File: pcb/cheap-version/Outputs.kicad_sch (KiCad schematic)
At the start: 21 parts, among them J501 FAN1 / 3.5 mm, J511 FAN2 / 3.5 mm, J521 PUMP 24V / 6W, Q501 AO3400A, Q511 AO3400A, Q521 AO3422

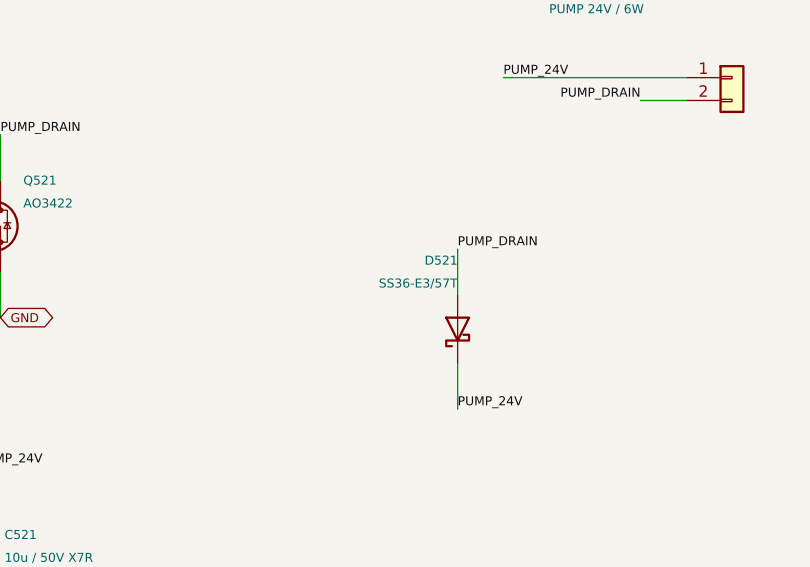
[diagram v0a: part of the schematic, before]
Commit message: cheap-version: schematic substitutions from stock parts
tools/make_cheap1.py generates the cheap-1 sheets from the PCB_V1 0.22 baseline:
ST1S14 for LMR16020 (RT resistor removed, EN/FB divider recalculated), IRS4427S and
IRL2505 for the heater, BSC146N10LS5 for the LED boost switches, SS56 diodes,
KF301/FS1.5/KF2510/XH connectors, stock resistors and capacitors (Source field =
stock:<id>). J901 XT60 is replaced by a screw terminal as decided. U101 TPS54202 and
D711/D721 SS5P10 are kept because datasheets for ST1S10 and SBRT15U100SP5 were not
available. ERC: 0 errors (one warning: footprint for the DTMSS-27 inductor pending);
netdiff against PCB_V1: no connectivity differences among untouched pins.

Co-Authored-By: Claude Sonnet 5.5 <noreply@anthropic.com>
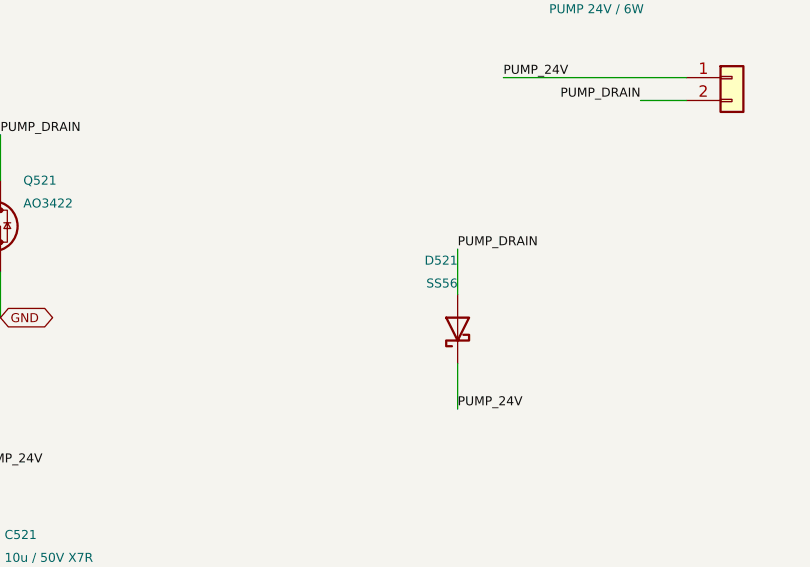
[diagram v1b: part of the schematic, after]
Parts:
- C521: LCSC C386166 -> C92388; MPN UMK325AB7106KMHP -> CL32B106KBJNNNE; Manufacturer Taiyo Yuden -> Samsung Electro-Mechanics; Source (none) -> stock:47
- D521: value SS36-E3/57T -> SS56; LCSC C35722 -> (none); MPN SS36-E3/57T -> SS56; Manufacturer Vishay -> (none); Source (none) -> stock:20
- J501, J511: footprint GrowBox:TerminalBlock_DORABO_DB125-3.5_1x04_P3.50mm_Horizontal -> Connector_Molex:Molex_KK-254_AE-6410-04A_1x04_P2.54mm_Vertical; LCSC C2757925 -> (none); MPN DB125-3.5-4P-GN-S -> KF2510-4P; Manufacturer DORABO -> (none); Source (none) -> stock:87
- J521: footprint GrowBox:TerminalBlock_DORABO_DB125-3.5_1x02_P3.50mm_Horizontal -> TerminalBlock_Phoenix:TerminalBlock_Phoenix_PT-1,5-2-3.5-H_1x02_P3.50mm_Horizontal; LCSC C466970 -> (none); MPN DB125-3.5-2P-GN-S -> FS1.5-02-350-2601R; Manufacturer DORABO -> (none); Source (none) -> stock:86
- R502, R512, R522: LCSC C25803 -> C14675; MPN 0603WAF1003T5E -> RC0603FR-07100KL; Manufacturer UNI-ROYAL -> Yageo; Source (none) -> stock:55
- R503, R513: MPN 0603WAF1001T5E -> RC0603FR-071KL; Manufacturer UNI-ROYAL -> Yageo; Source (none) -> stock:62
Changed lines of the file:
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@@
 	(title_block
 		(title "04 - Fans (12 V aux) and pump (24 V)")
-		(date "2026-09-30")
-		(rev "0.22-DRAFT")
+		(date "2026-10-03")
+		(rev "cheap-1-DRAFT")
 		(company "GrowBox controller")
-		(comment 1 "Simplified prototype; unrouted; hardware qualification pending")
+		(comment 1 "cheap-1: one-off board from stock parts, schematic derived from PCB_V1 0.22; unrouted")
 	)
 	(text "04  PTC 100 W — отдельный лист Heater"
@@
 			)
 		)
-		(property "Manufacturer" "UNI-ROYAL"
+		(property "Manufacturer" "Yageo"
 			(at 50.8 231.14 0)
 			(hide yes)
@@
 			)
 		)
-		(property "MPN" "0603WAF1003T5E"
+		(property "MPN" "RC0603FR-07100KL"
 			(at 50.8 231.14 0)
 			(hide yes)
@@
 			)
 		)
-		(property "LCSC" "C25803"
+		(property "LCSC" "C14675"
 			(at 50.8 231.14 0)
 			(hide yes)
@@
 					(size 1 1)
 				)
+				(justify left)
+			)
+		)
+		(property "Source" "stock:55"
+			(at 50.8 231.14 0)
+			(effects
+				(font
+					(size 1 1)
+				)
+				(hide yes)
 				(justify left)
 			)
@@
 			)
 		)
-		(property "Value" "SS36-E3/57T"
+		(property "Value" "SS56"
 			(at 154.94 214.63 90)
 			(show_name no)
@@
 			)
 		)
-		(property "LCSC" "C35722"
+		(property "LCSC" ""
 			(at 154.94 219.71 0)
 			(effects
@@
 			)
 		)
-		(property "MPN" "SS36-E3/57T"
+		(property "Source" "stock:20"
+			(at 154.94 219.71 90)
+			(effects
+				(font
+					(size 1 1)
+				)
+				(hide yes)
+				(justify left)
+			)
+		)
+		(property "MPN" "SS56"
 			(at 154.94 219.71 0)
 			(effects
@@
 			)
 		)
-		(property "Manufacturer" "Vishay"
+		(property "Manufacturer" ""
 			(at 154.94 219.71 0)
 			(effects
@@
 			)
 		)
-		(property "Footprint" "GrowBox:TerminalBlock_DORABO_DB125-3.5_1x04_P3.50mm_Horizontal"
+		(property "Footprint" "Connector_Molex:Molex_KK-254_AE-6410-04A_1x04_P2.54mm_Vertical"
 			(at 182.88 60.96 0)
 			(hide yes)
@@
 			)
 		)
-		(property "LCSC" "C2757925"
+		(property "LCSC" ""
 			(at 182.88 60.96 0)
 			(effects
@@
 			)
 		)
-		(property "MPN" "DB125-3.5-4P-GN-S"
+		(property "Source" "stock:87"
 			(at 182.88 60.96 0)
 			(effects
@@
 			)
 		)
-		(property "Manufacturer" "DORABO"
+		(property "MPN" "KF2510-4P"
+			(at 182.88 60.96 0)
+			(effects
+				(font
+					(size 1 1)
+				)
+				(hide yes)
+				(justify left)
+			)
+		)
+		(property "Manufacturer" ""
 			(at 182.88 60.96 0)
 			(effects
@@
 			)
 		)
-		(property "Manufacturer" "UNI-ROYAL"
+		(property "Manufacturer" "Yageo"
 			(at 50.8 93.98 0)
 			(hide yes)
@@
 			)
 		)
-		(property "MPN" "0603WAF1003T5E"
+		(property "MPN" "RC0603FR-07100KL"
 			(at 50.8 93.98 0)
 			(hide yes)
@@
 			)
 		)
-		(property "LCSC" "C25803"
+		(property "LCSC" "C14675"
 			(at 50.8 93.98 0)
 			(hide yes)
@@
 					(size 1 1)
 				)
+				(justify left)
+			)
+		)
+		(property "Source" "stock:55"
+			(at 50.8 93.98 0)
+			(effects
+				(font
+					(size 1 1)
+				)
+				(hide yes)
 				(justify left)
 			)
@@
 			)
 		)
-		(property "Footprint" "GrowBox:TerminalBlock_DORABO_DB125-3.5_1x02_P3.50mm_Horizontal"
+		(property "Footprint" "TerminalBlock_Phoenix:TerminalBlock_Phoenix_PT-1,5-2-3.5-H_1x02_P3.50mm_Horizontal"
 			(at 185.42 191.77 0)
 			(hide yes)
@@
 			)
 		)
-		(property "LCSC" "C466970"
+		(property "LCSC" ""
 			(at 185.42 191.77 0)
 			(effects
@@
 			)
 		)
-		(property "MPN" "DB125-3.5-2P-GN-S"
+		(property "Source" "stock:86"
 			(at 185.42 191.77 0)
 			(effects
@@
 			)
 		)
-		(property "Manufacturer" "DORABO"
+		(property "MPN" "FS1.5-02-350-2601R"
+			(at 185.42 191.77 0)
+			(effects
+				(font
+					(size 1 1)
+				)
+				(hide yes)
+				(justify left)
+			)
+		)
+		(property "Manufacturer" ""
 			(at 185.42 191.77 0)
 			(effects
@@
 			)
 		)
-		(property "Footprint" "GrowBox:TerminalBlock_DORABO_DB125-3.5_1x04_P3.50mm_Horizontal"
+		(property "Footprint" "Connector_Molex:Molex_KK-254_AE-6410-04A_1x04_P2.54mm_Vertical"
 			(at 381 60.96 0)
 			(hide yes)
@@
 			)
 		)
-		(property "LCSC" "C2757925"
+		(property "LCSC" ""
 			(at 381 60.96 0)
 			(effects
@@
 			)
 		)
-		(property "MPN" "DB125-3.5-4P-GN-S"
+		(property "Source" "stock:87"
 			(at 381 60.96 0)
 			(effects
@@
 			)
 		)
-		(property "Manufacturer" "DORABO"
+		(property "MPN" "KF2510-4P"
+			(at 381 60.96 0)
+			(effects
+				(font
+					(size 1 1)
+				)
+				(hide yes)
+				(justify left)
+			)
+		)
+		(property "Manufacturer" ""
 			(at 381 60.96 0)
 			(effects
@@
 			)
 		)
-		(property "Manufacturer" "UNI-ROYAL"
+		(property "Manufacturer" "Yageo"
 			(at 302.26 109.22 90)
 			(hide yes)
@@
 			)
 		)
-		(property "MPN" "0603WAF1001T5E"
+		(property "MPN" "RC0603FR-071KL"
 			(at 302.26 109.22 90)
 			(hide yes)
@@
 					(size 1 1)
 				)
+				(justify left)
+			)
+		)
+		(property "Source" "stock:62"
+			(at 302.26 109.22 90)
+			(effects
+				(font
+					(size 1 1)
+				)
+				(hide yes)
 				(justify left)
 			)
@@
 			)
 		)
-		(property "Manufacturer" "UNI-ROYAL"
+		(property "Manufacturer" "Yageo"
 			(at 248.92 93.98 0)
 			(hide yes)
@@
 			)
 		)
-		(property "MPN" "0603WAF1003T5E"
+		(property "MPN" "RC0603FR-07100KL"
 			(at 248.92 93.98 0)
 			(hide yes)
@@
 			)
 		)
-		(property "LCSC" "C25803"
+		(property "LCSC" "C14675"
 			(at 248.92 93.98 0)
 			(hide yes)
@@
 					(size 1 1)
 				)
+				(justify left)
+			)
+		)
+		(property "Source" "stock:55"
+			(at 248.92 93.98 0)
+			(effects
+				(font
+					(size 1 1)
+				)
+				(hide yes)
 				(justify left)
 			)
@@
 			)
 		)
-		(property "Manufacturer" "UNI-ROYAL"
+		(property "Manufacturer" "Yageo"
 			(at 104.14 109.22 90)
 			(hide yes)
@@
 			)
 		)
-		(property "MPN" "0603WAF1001T5E"
+		(property "MPN" "RC0603FR-071KL"
 			(at 104.14 109.22 90)
 			(hide yes)
@@
 					(size 1 1)
 				)
+				(justify left)
+			)
+		)
+		(property "Source" "stock:62"
+			(at 104.14 109.22 90)
+			(effects
+				(font
+					(size 1 1)
+				)
+				(hide yes)
 				(justify left)
 			)
@@
 			)
 		)
-		(property "LCSC" "C386166"
+		(property "LCSC" "C92388"
 			(at 101.6 243.84 0)
 			(effects
@@
 			)
 		)
-		(property "MPN" "UMK325AB7106KMHP"
+		(property "Source" "stock:47"
 			(at 101.6 243.84 0)
 			(effects
@@
 			)
 		)
-		(property "Manufacturer" "Taiyo Yuden"
+		(property "MPN" "CL32B106KBJNNNE"
 			(at 101.6 243.84 0)
 			(effects
+				(font
+					(size 1 1)
+				)
+				(hide yes)
+				(justify left)
+			)
+		)
+		(property "Manufacturer" "Samsung Electro-Mechanics"
+			(at 101.6 243.84 0)
+			(effects
